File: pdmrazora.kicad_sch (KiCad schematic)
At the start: 8 parts, among them J1 9-6437287-8, J2 M6_VBAT_GND

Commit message: Rename user-facing branding to PowerCore
Keep KiCad stem pdmrazora and Link Razor loom/connector compatibility.
No copper or routing changes; PCB title-block comment only.

Co-authored-by: Quintin <quintinbannink42@users.noreply.github.com>
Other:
- title: pdmrazora - Hellen-One Razor PDM frame -> pdmrazora - PowerCore PDM
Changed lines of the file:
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@@
 	(paper "A3")
 	(title_block
-		(title "pdmrazora - Hellen-One Razor PDM frame")
+		(title "pdmrazora - PowerCore PDM")
 		(date "2026-09-15")
 		(rev "a")
 		(company "quintinbannink42")
 		(comment 1 "https://github.com/quintinbannink42/hellen-pdm-razor")
-		(comment 2 "NOT HELLCORE - Hellen-One PDM matching Link Razor SuperSeal")
+		(comment 2 "PowerCore PDM; Link Razor SuperSeal loom - NOT HELLCORE")
 		(comment 3 "MCU: mega-mcu144 >= 0.7")
 	)

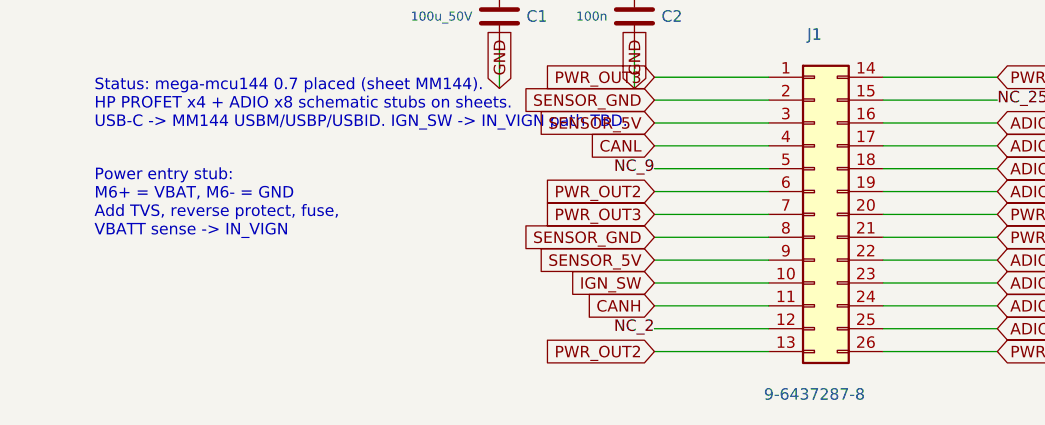
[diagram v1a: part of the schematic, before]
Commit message: Redesign PowerCore floorplan: M6 bobbins, 104x93, vertical SuperSeal EMI split
Replace the J2 2.54 mm pin-header with M6 bolt-through bobbins, shrink
Edge.Cuts to Link Razor-class 104x93 mm (aux origin at bottom-left), place
a vertical SuperSeal as an EMI wall between mega-mcu144 and the PROFET
power half, and align the M1000 keepout/value with hellen-one 0.7.

Old Manhattan copper is dropped with the move; coarse VBAT/GND pours remain
for the new outline. EN/IS/ADIO routing is left as human copper polish.

Co-authored-by: Quintin <quintinbannink42@users.noreply.github.com>
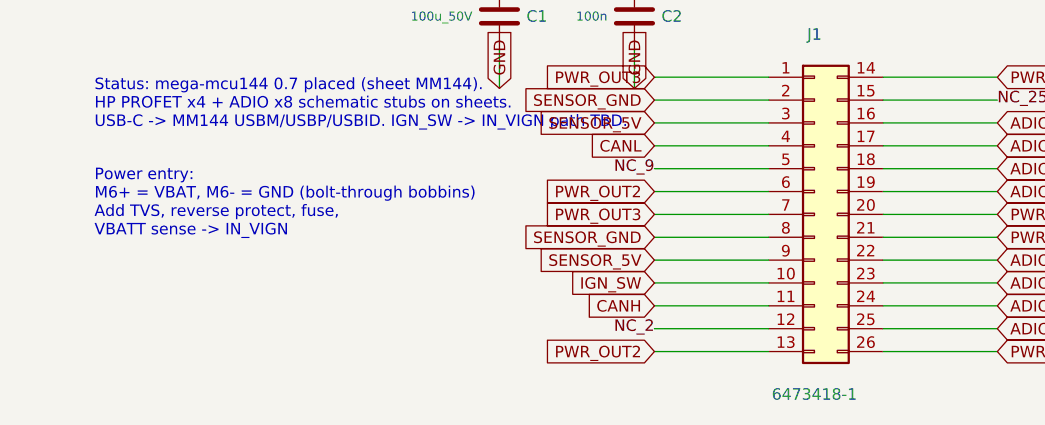
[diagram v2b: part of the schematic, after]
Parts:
- J1: value 9-6437287-8 -> 6473418-1; footprint pdmrazora:TE_9-6437287-8_SuperSeal26 -> pdmrazora:TE_6473418-1_SuperSeal26_Vertical
- J2: footprint Connector_PinHeader_2.54mm:PinHeader_1x02_P2.54mm_Vertical -> pdmrazora:M6_BoltThrough_Bobbin_x2
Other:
- note added: "Power entry: M6+ = VBAT, M6- = GND (bolt-through bobbins) Add TVS, reverse protect, fuse, VBATT sense -> IN_VIGN"
- note removed: "Power entry stub: M6+ = VBAT, M6- = GND Add TVS, reverse protect, fuse, VBATT sense -> IN_VIGN"
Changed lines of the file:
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@@
 			)
 		)
-		(property "Value" "9-6437287-8"
+		(property "Value" "6473418-1"
 			(at 100 130 0)
 			(effects
@@
 			)
 		)
-		(property "Footprint" "pdmrazora:TE_9-6437287-8_SuperSeal26"
+		(property "Footprint" "pdmrazora:TE_6473418-1_SuperSeal26_Vertical"
 			(at 100 110 0)
 			(effects
@@
 			)
 		)
-		(property "Datasheet" "https://www.te.com/en/product-9-6437287-8.html"
+		(property "Datasheet" "https://www.te.com/en/product-6473418-1.html"
 			(at 100 110 0)
 			(effects
@@
 			)
 		)
-		(property "Description" "TE/AMP SuperSeal 1.0 26pos RA Au keying1 (9-6437287-8); Link Connector C"
+		(property "Description" "TE/AMP SuperSeal 1.0 26pos vertical Au (6473418-1); Link Connector C pin numbers"
 			(at 100 110 0)
 			(effects
@@
 			)
 		)
-		(property "Footprint" "Connector_PinHeader_2.54mm:PinHeader_1x02_P2.54mm_Vertical"
+		(property "Footprint" "pdmrazora:M6_BoltThrough_Bobbin_x2"
 			(at 35 35 0)
 			(effects
@@
 			)
 		)
-		(property "Description" "M6 main power stubs VBAT+ / GND"
+		(property "Description" "M6 bolt-through bobbins VBAT+ / GND, 25 mm pitch"
 			(at 35 35 0)
 			(effects
@@
 		)
 	)
-	(text "Power entry stub:\nM6+ = VBAT, M6- = GND\nAdd TVS, reverse protect, fuse,\nVBATT sense -> IN_VIGN"
+	(text "Power entry:\nM6+ = VBAT, M6- = GND (bolt-through bobbins)\nAdd TVS, reverse protect, fuse,\nVBATT sense -> IN_VIGN"
 		(at 20 105 0)
 		(effects

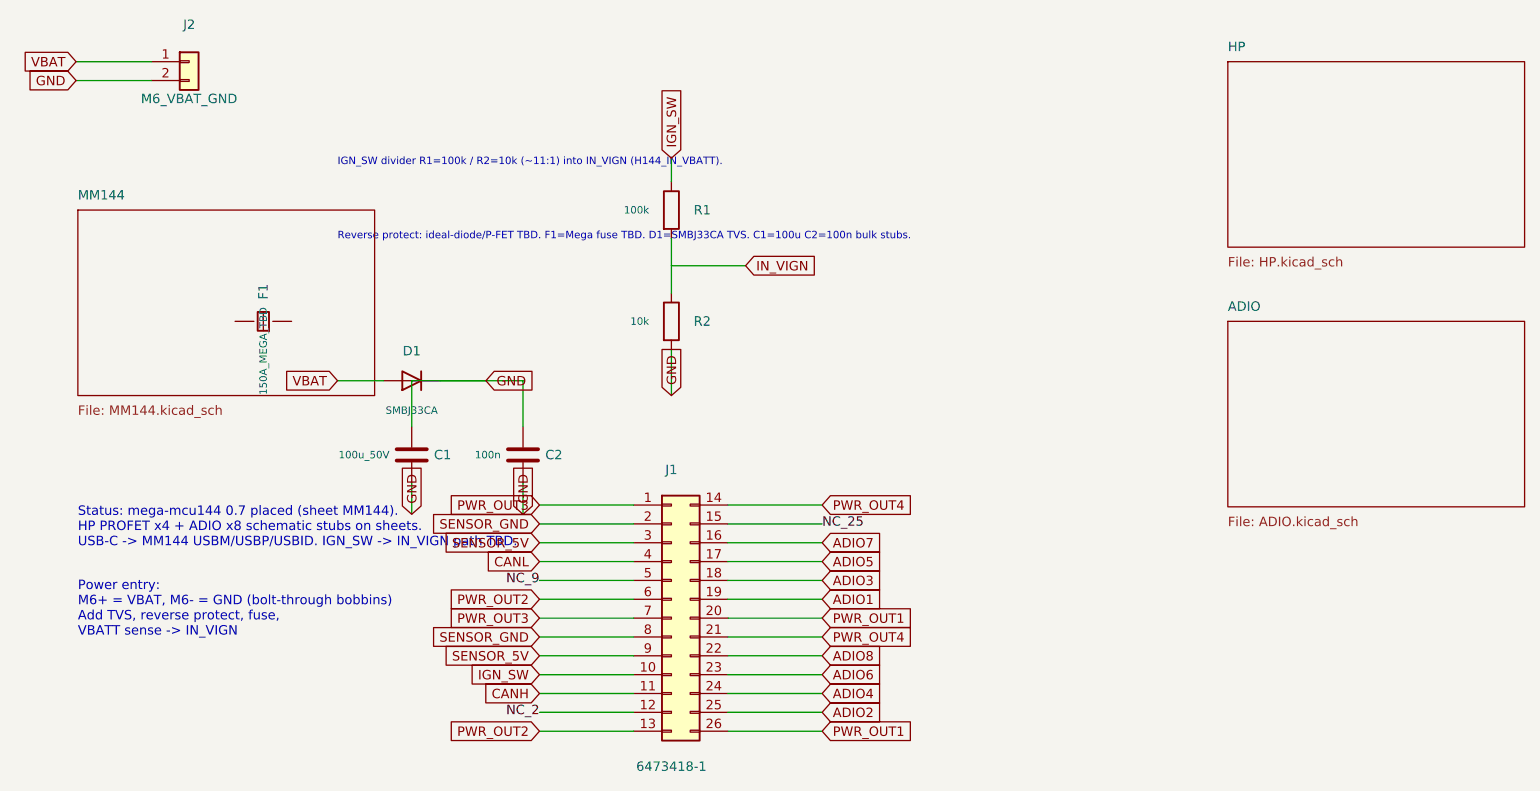
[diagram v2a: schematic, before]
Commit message: Split VBAT/GND M6 bobbins onto opposite power-field edges
Replace the 25 mm dual-bobbin J2 with two independent single M6
footprints so VBAT+ (north) and GND (south) are no longer paired on
the east edge, and neither shares the mega-mcu144 west side. HP and
ADIO sit between them. Razor-class 104x93 outline and vertical
SuperSeal EMI wall are unchanged. Paired-spine copper is stripped;
zone outlines await a follow-up fill.

Co-authored-by: Quintin <quintinbannink42@users.noreply.github.com>
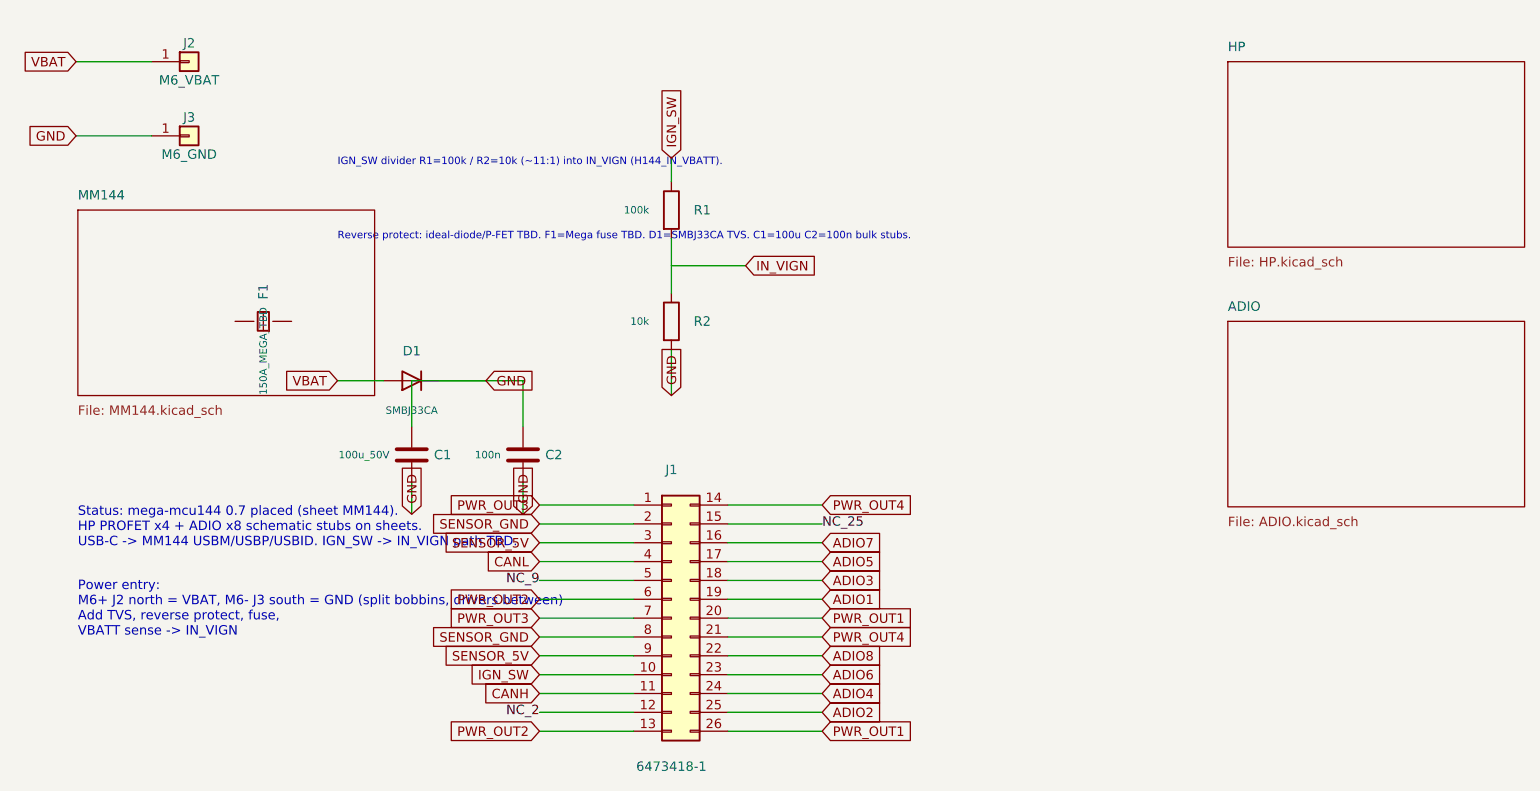
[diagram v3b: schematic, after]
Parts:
- added J3: M6_GND, pdmrazora:M6_BoltThrough_Bobbin, symbol Connector_Generic:Conn_01x01
- J2: value M6_VBAT_GND -> M6_VBAT; footprint pdmrazora:M6_BoltThrough_Bobbin_x2 -> pdmrazora:M6_BoltThrough_Bobbin; symbol Connector_Generic:Conn_01x02 -> Connector_Generic:Conn_01x01
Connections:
- net GND: now also J3.1 (Pin_1); no longer J2.2 (Pin_2)
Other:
- note added: "Power entry: M6+ J2 north = VBAT, M6- J3 south = GND (split bobbins, drivers between) Add TVS, reverse protect, fuse, VBATT sense -> IN_VIGN"
- note removed: "Power entry: M6+ = VBAT, M6- = GND (bolt-through bobbins) Add TVS, reverse protect, fuse, VBATT sense -> IN_VIGN"
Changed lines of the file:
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@@
 	)
 	(symbol
-		(lib_id "Connector_Generic:Conn_01x02")
+		(lib_id "Connector_Generic:Conn_01x01")
 		(at 35 35 0)
 		(unit 1)
@@
 		(dnp no)
 		(property "Reference" "J2"
-			(at 35 30 0)
+			(at 35 32.5 0)
 			(effects
 				(font
@@
 			)
 		)
-		(property "Value" "M6_VBAT_GND"
-			(at 35 40 0)
+		(property "Value" "M6_VBAT"
+			(at 35 37.5 0)
 			(effects
 				(font
@@
 			)
 		)
-		(property "Footprint" "pdmrazora:M6_BoltThrough_Bobbin_x2"
+		(property "Footprint" "pdmrazora:M6_BoltThrough_Bobbin"
 			(at 35 35 0)
 			(effects
@@
 			)
 		)
-		(property "Description" "M6 bolt-through bobbins VBAT+ / GND, 25 mm pitch"
+		(property "Description" "M6 bolt-through bobbin VBAT+ (north power-field edge)"
 			(at 35 35 0)
 			(effects
@@
 		)
 		(pin "1"
-		)
-		(pin "2"
 		)
 	)
@@
 		)
 	)
+	(symbol
+		(lib_id "Connector_Generic:Conn_01x01")
+		(at 35 45 0)
+		(unit 1)
+		(exclude_from_sim no)
+		(in_bom yes)
+		(on_board yes)
+		(dnp no)
+		(property "Reference" "J3"
+			(at 35 42.5 0)
+			(effects
+				(font
+					(size 1.27 1.27)
+				)
+			)
+		)
+		(property "Value" "M6_GND"
+			(at 35 47.5 0)
+			(effects
+				(font
+					(size 1.27 1.27)
+				)
+			)
+		)
+		(property "Footprint" "pdmrazora:M6_BoltThrough_Bobbin"
+			(at 35 45 0)
+			(effects
+				(font
+					(size 1.27 1.27)
+				)
+				(hide yes)
+			)
+		)
+		(property "Datasheet" "~"
+			(at 35 45 0)
+			(effects
+				(font
+					(size 1.27 1.27)
+				)
+				(hide yes)
+			)
+		)
+		(property "Description" "M6 bolt-through bobbin GND (south power-field edge)"
+			(at 35 45 0)
+			(effects
+				(font
+					(size 1.27 1.27)
+				)
+				(hide yes)
+			)
+		)
+		(pin "1"
+		)
+	)
 	(wire
-		(pts (xy 29.92 37.54) (xy 19.76 37.54))
+		(pts (xy 29.92 45.0) (xy 19.76 45.0))
 		(stroke
 			(width 0)
@@
 	)
 	(global_label "GND"
-		(at 19.76 37.54 0)
+		(at 19.76 45.0 0)
 		(shape input)
 		(effects
@@
 		)
 	)
-	(text "Power entry:\nM6+ = VBAT, M6- = GND (bolt-through bobbins)\nAdd TVS, reverse protect, fuse,\nVBATT sense -> IN_VIGN"
+	(text "Power entry:\nM6+ J2 north = VBAT, M6- J3 south = GND (split bobbins, drivers between)\nAdd TVS, reverse protect, fuse,\nVBATT sense -> IN_VIGN"
 		(at 20 105 0)
 		(effects

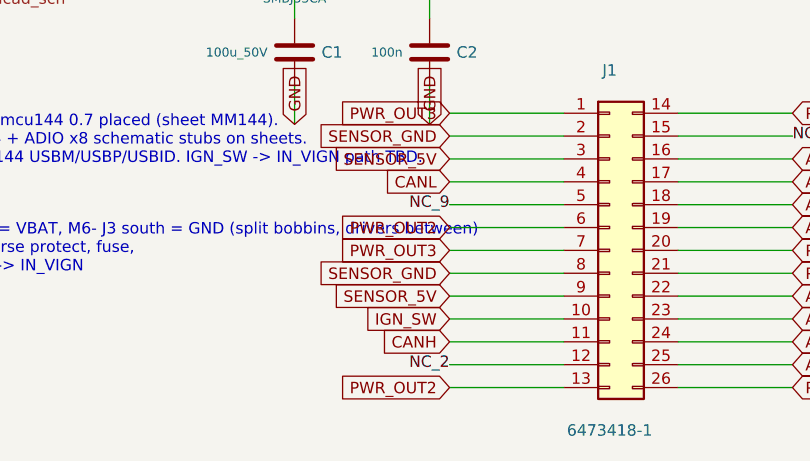
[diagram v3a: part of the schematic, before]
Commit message: Pour ADIO2 at 4.53 mm through SuperSeal NC pins 2 and 9.
Same-net copper on the unused pads opens one even channel above the
1 oz 8 A line. ADIO4, ADIO6, and ADIO8 stay short of 3.47 mm; pin 25
stays N/C. Hard DRC stays 0.

Co-authored-by: Quintin <quintinbannink42@users.noreply.github.com>
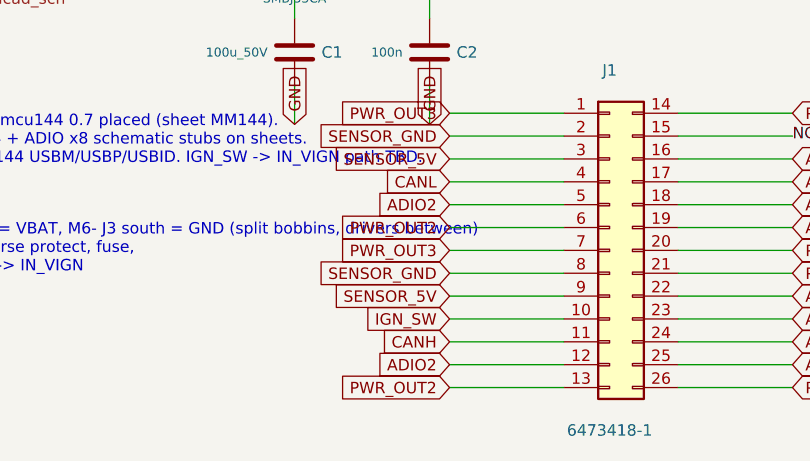
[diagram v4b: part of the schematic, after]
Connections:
- net NC_2 is gone; now on net ADIO2: J1.12 (Pin_12)
- net NC_9 is gone; now on net ADIO2: J1.5 (Pin_5)
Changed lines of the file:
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@@
 		)
 	)
-	(label "NC_2"
+	(global_label "ADIO2"
 		(at 82.22 122.7 0)
+		(shape input)
 		(effects
 			(font
@@
 		)
 	)
-	(label "NC_9"
+	(global_label "ADIO2"
 		(at 82.22 104.92 0)
+		(shape input)
 		(effects
 			(font
